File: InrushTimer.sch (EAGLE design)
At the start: 71 parts, among them IC2 TLC272D, IC3 4076N, IC6 555, Q2 TIP41C

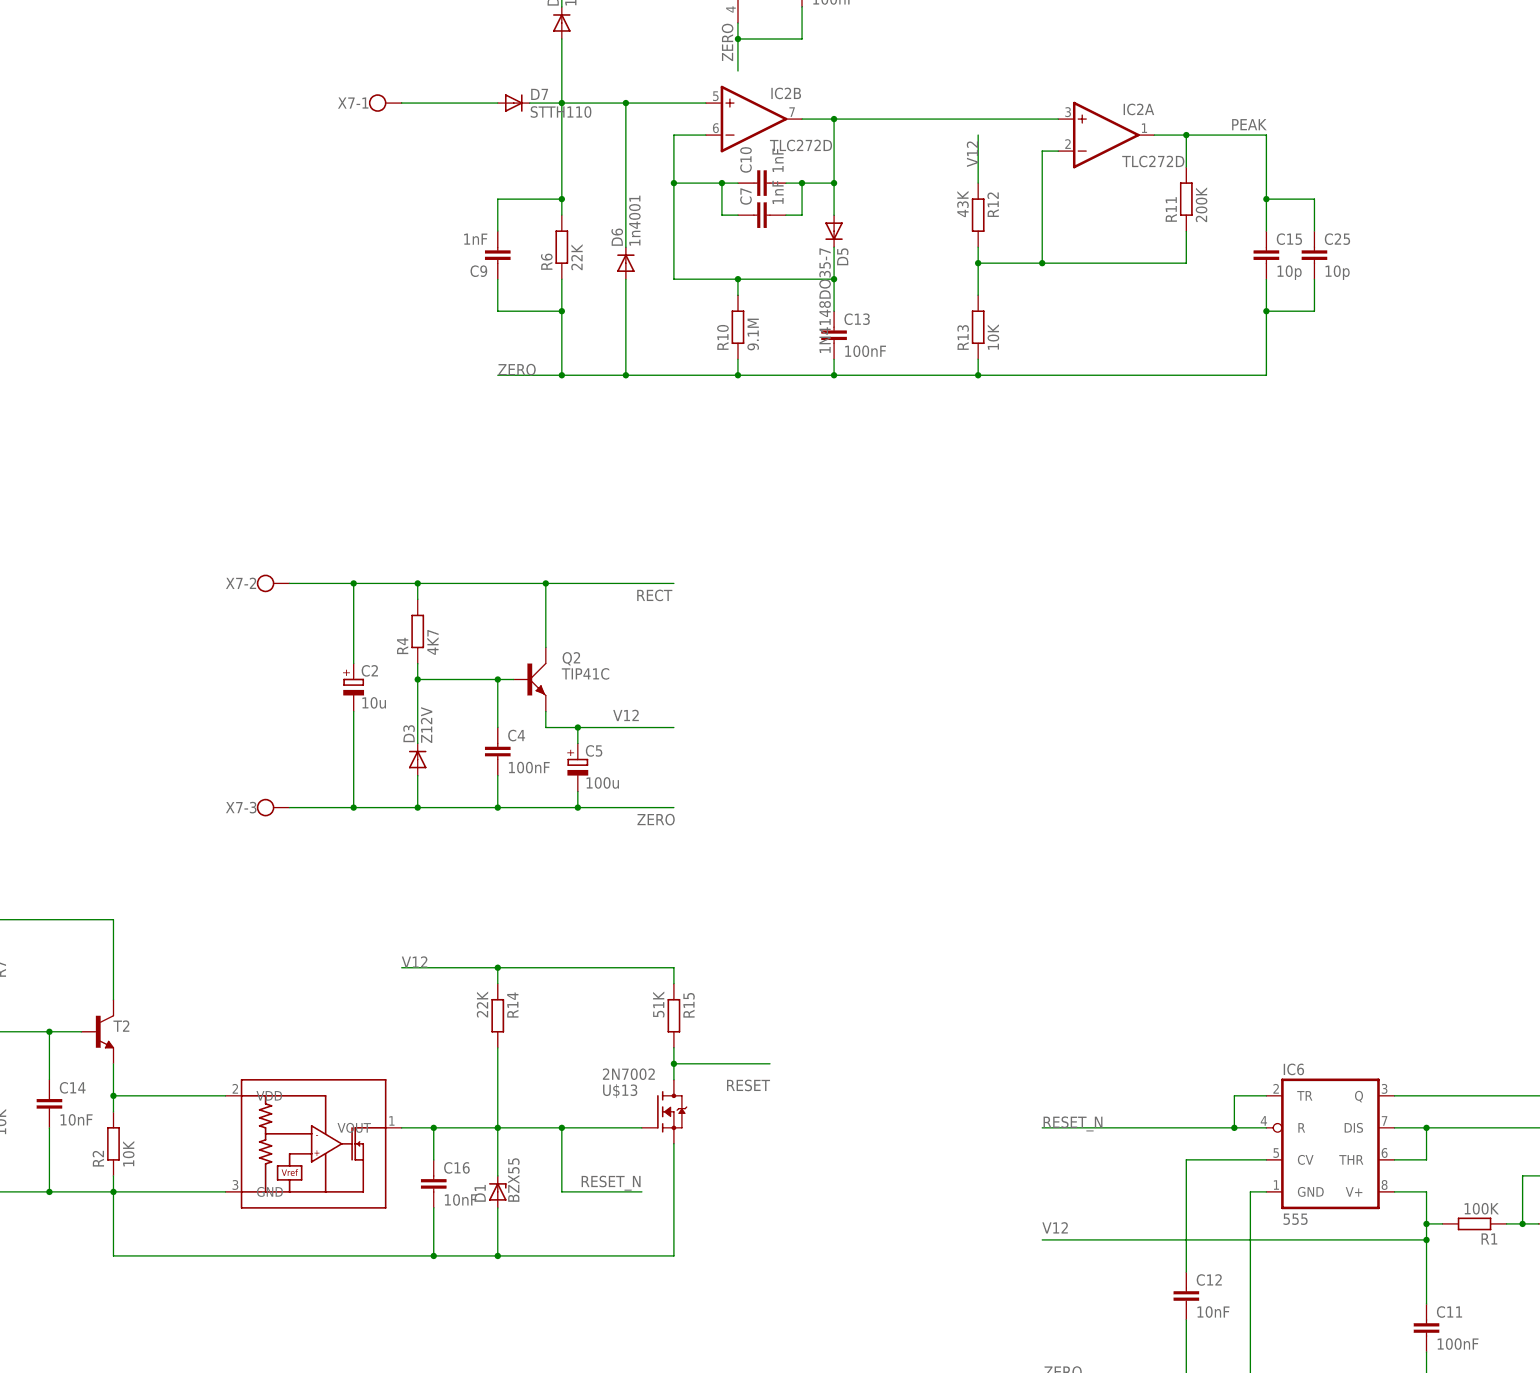
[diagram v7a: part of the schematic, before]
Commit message: Added inductor model and tweaked schematic.
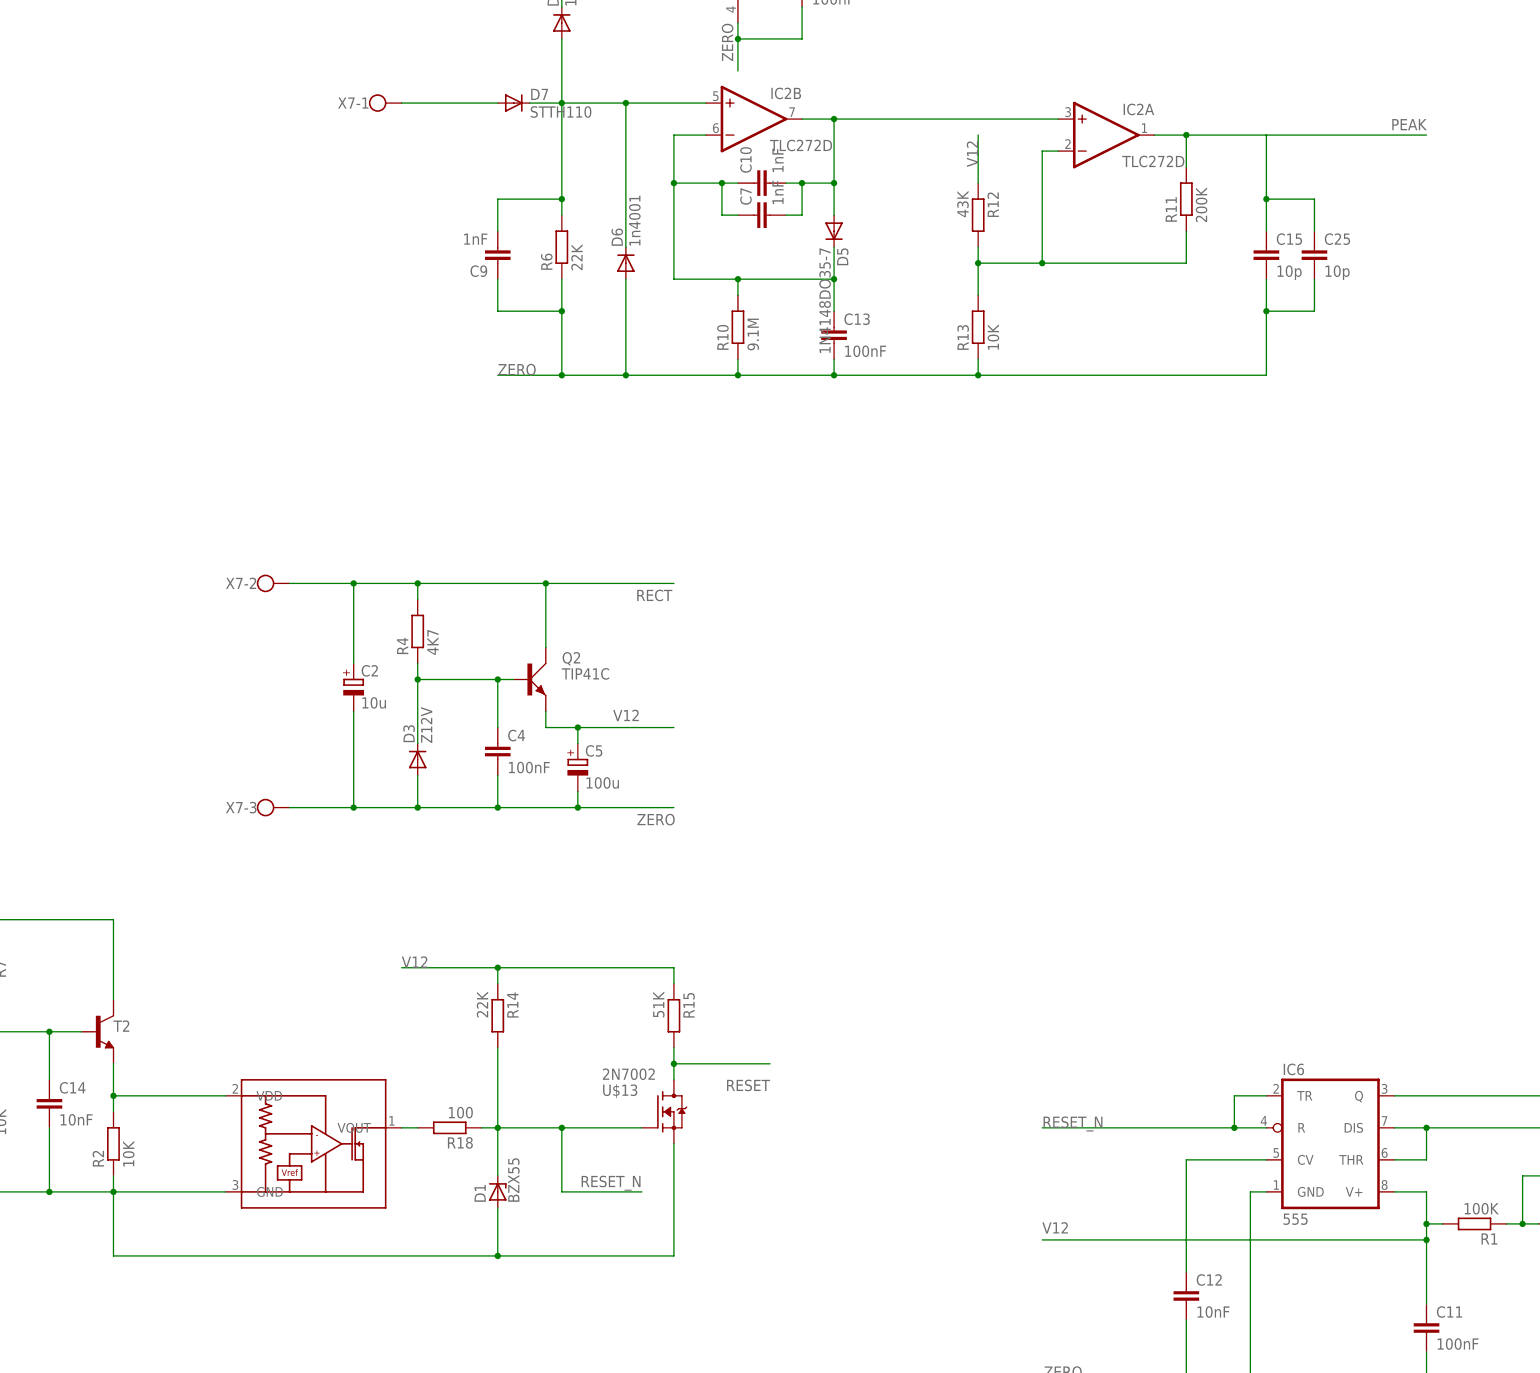
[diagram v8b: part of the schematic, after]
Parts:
- removed C16: 10nF, rcl:C-EU050-024X044
- added R18: 100, rcl:R-EU_0207/2V
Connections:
- new net N$23: R18.2, U$4.VOUT
- net RESET_N: now also R18.1; no longer C16.1, U$4.VOUT
- net ZERO: no longer C16.2
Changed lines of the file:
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@@
 <setting verticaltext="up"/>
 </settings>
-<grid distance="0.1" unitdist="inch" unit="inch" style="lines" multiple="1" display="no" altdistance="0.01" altunitdist="inch" altunit="inch"/>
+<grid distance="0.1" unitdist="inch" unit="inch" style="lines" multiple="1" display="yes" altdistance="0.01" altunitdist="inch" altunit="inch"/>
 <layers>
 <layer number="1" name="Top" color="4" fill="1" visible="no" active="no"/>
@@
 <part name="C9" library="rcl" deviceset="C-EU" device="C0805K" value="1nF"/>
 <part name="C14" library="rcl" deviceset="C-EU" device="050-024X044" value="10nF"/>
-<part name="C16" library="rcl" deviceset="C-EU" device="050-024X044" value="10nF"/>
 <part name="C10" library="rcl" deviceset="C-EU" device="C0805K" value="1nF"/>
 <part name="C1" library="rcl" deviceset="C-EU" device="C1206K" value="100nF"/>
@@
 <part name="R3" library="rcl" deviceset="R-EU_" device="0207/2V" value="10K"/>
 <part name="R5" library="rcl" deviceset="R-EU_" device="0207/2V" value="10K"/>
+<part name="R18" library="rcl" deviceset="R-EU_" device="0207/2V" value="100"/>
 </parts>
 <sheets>
@@
 <instance part="C9" gate="G$1" x="78.74" y="116.84" rot="R180"/>
 <instance part="C14" gate="G$1" x="7.62" y="-15.24"/>
-<instance part="C16" gate="G$1" x="68.58" y="-27.94"/>
 <instance part="C10" gate="G$1" x="119.38" y="129.54" rot="R90"/>
 <instance part="C1" gate="G$1" x="127" y="162.56"/>
@@
 <instance part="R3" gate="G$1" x="388.62" y="12.7" rot="R180"/>
 <instance part="R5" gate="G$1" x="388.62" y="7.62" rot="R180"/>
+<instance part="R18" gate="G$1" x="71.12" y="-20.32" rot="R180"/>
 </instances>
 <busses>
@@
 <wire x1="78.74" y1="-40.64" x2="78.74" y2="-33.02" width="0.1524" layer="91"/>
 <junction x="78.74" y="-40.64"/>
-<wire x1="78.74" y1="-40.64" x2="68.58" y2="-40.64" width="0.1524" layer="91"/>
 <pinref part="D1" gate="1" pin="A"/>
-<pinref part="C16" gate="G$1" pin="2"/>
-<wire x1="68.58" y1="-33.02" x2="68.58" y2="-40.64" width="0.1524" layer="91"/>
 <pinref part="D12" gate="1" pin="A"/>
 <wire x1="-12.7" y1="-30.48" x2="-25.4" y2="-30.48" width="0.1524" layer="91"/>
@@
 <wire x1="-2.54" y1="-30.48" x2="-12.7" y2="-30.48" width="0.1524" layer="91"/>
 <wire x1="35.56" y1="-30.48" x2="17.78" y2="-30.48" width="0.1524" layer="91"/>
-<wire x1="68.58" y1="-40.64" x2="17.78" y2="-40.64" width="0.1524" layer="91"/>
+<wire x1="78.74" y1="-40.64" x2="17.78" y2="-40.64" width="0.1524" layer="91"/>
 <wire x1="17.78" y1="-40.64" x2="17.78" y2="-30.48" width="0.1524" layer="91"/>
-<junction x="68.58" y="-40.64"/>
 <junction x="17.78" y="-30.48"/>
 <pinref part="R2" gate="G$1" pin="1"/>
@@
 <segment>
 <wire x1="200.66" y1="137.16" x2="187.96" y2="137.16" width="0.1524" layer="91"/>
-<label x="200.66" y="139.7" size="1.778" layer="95" rot="R180"/>
+<label x="226.06" y="139.7" size="1.778" layer="95" rot="R180"/>
 <pinref part="R11" gate="G$1" pin="2"/>
 <wire x1="187.96" y1="132.08" x2="187.96" y2="137.16" width="0.1524" layer="91"/>
@@
 <wire x1="187.96" y1="137.16" x2="182.88" y2="137.16" width="0.1524" layer="91"/>
 <junction x="187.96" y="137.16"/>
+<wire x1="200.66" y1="137.16" x2="226.06" y2="137.16" width="0.1524" layer="91"/>
 </segment>
 </net>
@@
 </segment>
 <segment>
-<pinref part="U$4" gate="G$1" pin="VOUT"/>
 <pinref part="U$13" gate="G$1" pin="G"/>
-<wire x1="63.5" y1="-20.32" x2="68.58" y2="-20.32" width="0.1524" layer="91"/>
-<wire x1="68.58" y1="-20.32" x2="78.74" y2="-20.32" width="0.1524" layer="91"/>
 <wire x1="78.74" y1="-20.32" x2="88.9" y2="-20.32" width="0.1524" layer="91"/>
 <wire x1="88.9" y1="-20.32" x2="101.6" y2="-20.32" width="0.1524" layer="91"/>
@@
 <junction x="78.74" y="-20.32"/>
 <pinref part="D1" gate="1" pin="C"/>
-<pinref part="C16" gate="G$1" pin="1"/>
-<wire x1="68.58" y1="-25.4" x2="68.58" y2="-20.32" width="0.1524" layer="91"/>
-<junction x="68.58" y="-20.32"/>
 <pinref part="R14" gate="G$1" pin="2"/>
 <wire x1="78.74" y1="-7.62" x2="78.74" y2="-20.32" width="0.1524" layer="91"/>
@@
 <junction x="88.9" y="-20.32"/>
 <wire x1="88.9" y1="-30.48" x2="101.6" y2="-30.48" width="0.1524" layer="91"/>
+<pinref part="R18" gate="G$1" pin="1"/>
+<wire x1="78.74" y1="-20.32" x2="76.2" y2="-20.32" width="0.1524" layer="91"/>
 </segment>
 </net>
@@
 </segment>
 </net>
+<net name="N$23" class="0">
+<segment>
+<pinref part="R18" gate="G$1" pin="2"/>
+<pinref part="U$4" gate="G$1" pin="VOUT"/>
+<wire x1="66.04" y1="-20.32" x2="63.5" y2="-20.32" width="0.1524" layer="91"/>
+</segment>
+</net>
